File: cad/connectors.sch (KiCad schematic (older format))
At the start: 21 parts, among them J201 JACK_IN, J202 JACK_OUT, J203 CONN_PSU, J204 SW_BYPASS, J205 SW_FAT_A, J206 SW_EQ_A, J207 CONN_SIGNALS_A, J208 CONN_SW_EQ_A, K201 TQ2SA-5V, Q201 DTC123Y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

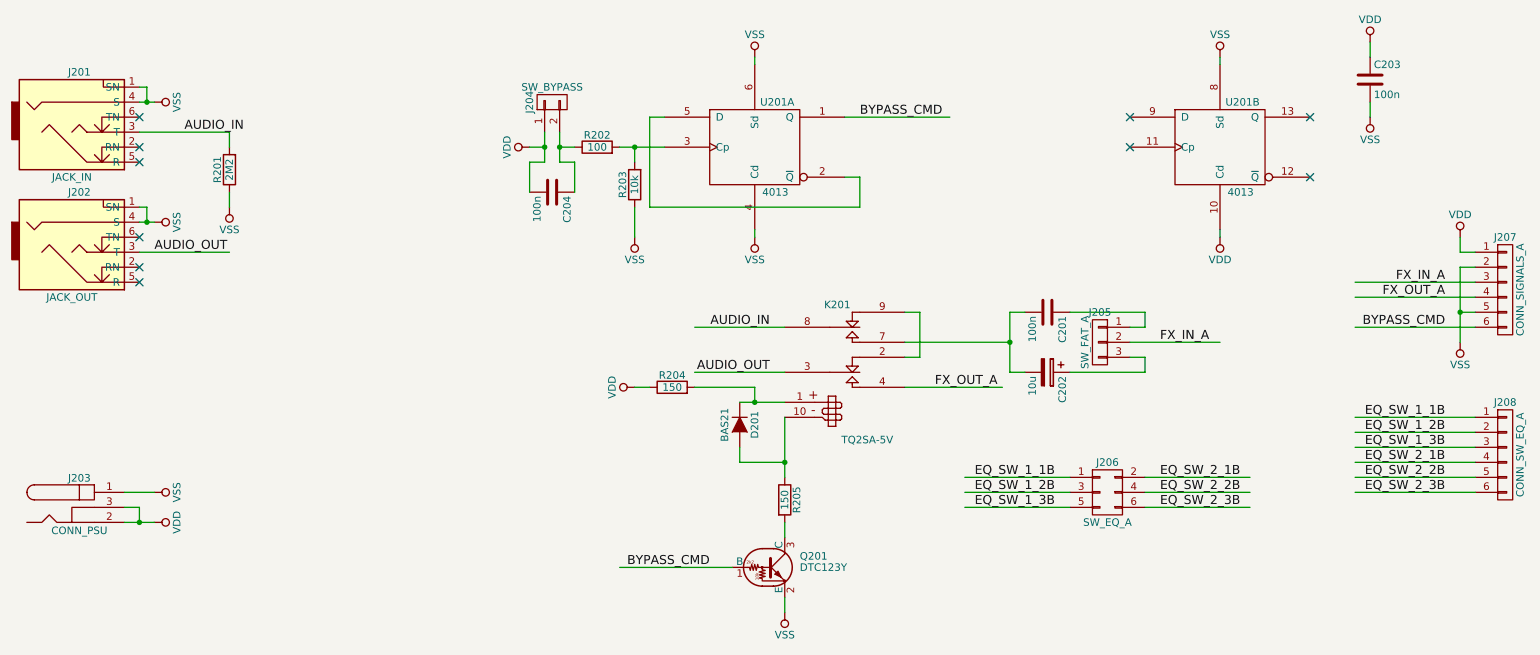
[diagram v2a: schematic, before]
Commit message: Corrected layout
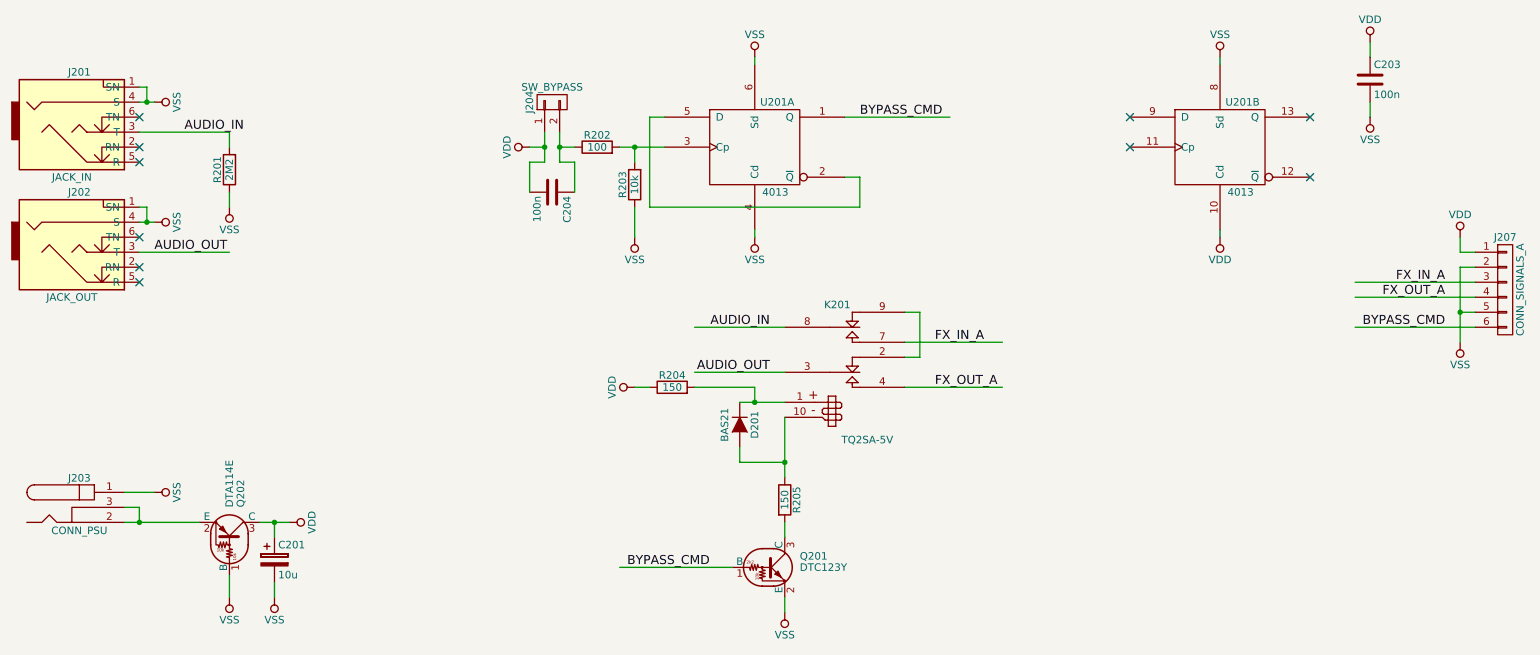
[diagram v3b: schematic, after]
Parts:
- removed C201: 100n, Capacitors_SMD:C_0603, symbol C
- removed C202: 10u, Capacitors_SMD:CP_Elec_4x4.5, symbol CP
- removed J205: SW_FAT_A, flax_lib:SW_SPDT_through_hole, symbol CONN_01X03
- removed J206: SW_EQ_A, flax_lib:SW_DPDT_through_hole, symbol CONN_02X03
- removed J208: CONN_SW_EQ_A, Pin_Headers:Pin_Header_Straight_1x06_Pitch1.27mm, symbol CONN_01X06
- added C201: 10u, Capacitors_SMD:CP_Elec_4x4.5, symbol CP
- added Q202: DTA114E, TO_SOT_Packages_SMD:SOT-23, symbol DTA114E
- J207: footprint Pin_Headers:Pin_Header_Straight_1x06_Pitch1.27mm -> Pin_Headers:Pin_Header_Straight_1x06_Pitch2.54mm
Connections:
- net labels removed: EQ_SW_1_1B, EQ_SW_1_2B, EQ_SW_1_3B, EQ_SW_2_1B, EQ_SW_2_2B, EQ_SW_2_3B
- wire segments 84 -> 66
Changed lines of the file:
@@
 LIBS:contrib
 LIBS:valves
+LIBS:flax_lib
 LIBS:hot_silicon_fuzz-cache
 EELAYER 25 0
@@
 L VDD #PWR02
 U 1 1 599D5C70
-P 1700 3900
-F 0 "#PWR02" H 1700 3750 50  0001 C CNN
-F 1 "VDD" H 1700 4050 50  0000 C CNN
-F 2 "" H 1700 3900 50  0001 C CNN
-F 3 "" H 1700 3900 50  0001 C CNN
-	1    1700 3900
+P 2600 3900
+F 0 "#PWR02" H 2600 3750 50  0001 C CNN
+F 1 "VDD" H 2600 4050 50  0000 C CNN
+F 2 "" H 2600 3900 50  0001 C CNN
+F 3 "" H 2600 3900 50  0001 C CNN
+	1    2600 3900
 	0    1    1    0
 $EndComp
@@
 Text Label 10300 2600 2    60   ~ 0
 BYPASS_CMD
-Text Label 8400 2700 0    60   ~ 0
+Text Label 6900 2700 0    60   ~ 0
 FX_IN_A
 Text Label 6900 3000 0    60   ~ 0
@@
 Text Label 5800 2900 2    60   ~ 0
 AUDIO_OUT
-$Comp
-L CONN_01X03 J205
-U 1 1 599E0F67
-P 8000 2700
-F 0 "J205" H 8000 2900 50  0000 C CNN
-F 1 "SW_FAT_A" V 8100 2700 50  0000 C CNN
-F 2 "flax_lib:SW_SPDT_through_hole" H 8000 2700 50  0001 C CNN
-F 3 "" H 8000 2700 50  0001 C CNN
-	1    8000 2700
-	-1   0    0    -1
-$EndComp
 Text Label 1900 1300 0    60   ~ 0
 AUDIO_IN
@@
 	1700 1100 1600 1100
 Wire Wire Line
-	1700 3900 1500 3900
+	1500 3900 2000 3900
 Wire Wire Line
 	1700 3700 1500 3700
@@
 Wire Wire Line
 	6800 2800 6700 2800
-Wire Wire Line
-	6700 2700 7400 2700
 Wire Wire Line
 	6700 3000 7350 3000
@@
 	1650 1800 1600 1800
 Connection ~ 1650 1900
-$Comp
-L C C201
-U 1 1 59A4C299
-P 7650 2500
-F 0 "C201" H 7675 2600 50  0000 L CNN
-F 1 "100n" H 7675 2400 50  0000 L CNN
-F 2 "Capacitors_SMD:C_0603" H 7688 2350 50  0001 C CNN
-F 3 "" H 7650 2500 50  0001 C CNN
-	1    7650 2500
-	0    1    1    0
-$EndComp
-Wire Wire Line
-	7400 2500 7400 2900
-Wire Wire Line
-	7400 2500 7500 2500
-$Comp
-L CP C202
-U 1 1 59A4C4B8
-P 7650 2900
-F 0 "C202" H 7675 3000 50  0000 L CNN
-F 1 "10u" H 7675 2800 50  0000 L CNN
-F 2 "Capacitors_SMD:CP_Elec_4x4.5" H 7688 2750 50  0001 C CNN
-F 3 "" H 7650 2900 50  0001 C CNN
-	1    7650 2900
-	0    1    1    0
-$EndComp
-Wire Wire Line
-	7400 2900 7500 2900
-Connection ~ 7400 2700
-Wire Wire Line
-	8200 2700 8800 2700
-Wire Wire Line
-	8200 2600 8300 2600
-Wire Wire Line
-	8300 2600 8300 2500
-Wire Wire Line
-	8300 2500 7800 2500
-Wire Wire Line
-	7800 2900 8300 2900
-Wire Wire Line
-	8300 2900 8300 2800
-Wire Wire Line
-	8300 2800 8200 2800
 Wire Wire Line
 	9700 2300 10500 2300
@@
 F 0 "J207" H 10700 2700 50  0000 C CNN
 F 1 "CONN_SIGNALS_A" V 10800 2350 50  0000 C CNN
-F 2 "Pin_Headers:Pin_Header_Straight_1x06_Pitch1.27mm" H 10700 2350 50  0001 C CNN
+F 2 "Pin_Headers:Pin_Header_Straight_1x06_Pitch2.54mm" H 10700 2350 50  0001 C CNN
 F 3 "" H 10700 2350 50  0001 C CNN
 	1    10700 2350
@@
 	10500 2500 10400 2500
 Connection ~ 10400 2500
-Text Label 10300 3200 2    60   ~ 0
-EQ_SW_1_1B
-$Comp
-L CONN_01X06 J208
-U 1 1 59A529D0
-P 10700 3450
-F 0 "J208" H 10700 3800 50  0000 C CNN
-F 1 "CONN_SW_EQ_A" V 10800 3450 50  0000 C CNN
-F 2 "Pin_Headers:Pin_Header_Straight_1x06_Pitch1.27mm" H 10700 3450 50  0001 C CNN
-F 3 "" H 10700 3450 50  0001 C CNN
-	1    10700 3450
-	1    0    0    -1
-$EndComp
-Wire Wire Line
-	10500 3200 9700 3200
-Text Label 10300 3300 2    60   ~ 0
-EQ_SW_1_2B
-Text Label 10300 3400 2    60   ~ 0
-EQ_SW_1_3B
-Text Label 10300 3500 2    60   ~ 0
-EQ_SW_2_1B
-Wire Wire Line
-	10500 3500 9700 3500
-Text Label 10300 3600 2    60   ~ 0
-EQ_SW_2_2B
-Text Label 10300 3700 2    60   ~ 0
-EQ_SW_2_3B
-Wire Wire Line
-	10500 3300 9700 3300
-Wire Wire Line
-	9700 3400 10500 3400
-Wire Wire Line
-	10500 3600 9700 3600
-Wire Wire Line
-	9700 3700 10500 3700
-$Comp
-L CONN_02X03 J206
-U 1 1 59A53228
-P 8050 3700
-F 0 "J206" H 8050 3900 50  0000 C CNN
-F 1 "SW_EQ_A" H 8050 3500 50  0000 C CNN
-F 2 "flax_lib:SW_DPDT_through_hole" H 8050 2500 50  0001 C CNN
-F 3 "" H 8050 2500 50  0001 C CNN
-	1    8050 3700
-	1    0    0    -1
-$EndComp
-Text Label 7700 3600 2    60   ~ 0
-EQ_SW_1_1B
-Text Label 7700 3700 2    60   ~ 0
-EQ_SW_1_2B
-Text Label 7700 3800 2    60   ~ 0
-EQ_SW_1_3B
-Text Label 8400 3600 0    60   ~ 0
-EQ_SW_2_1B
-Text Label 8400 3700 0    60   ~ 0
-EQ_SW_2_2B
-Text Label 8400 3800 0    60   ~ 0
-EQ_SW_2_3B
-Wire Wire Line
-	7800 3600 7100 3600
-Wire Wire Line
-	7100 3700 7800 3700
-Wire Wire Line
-	7800 3800 7100 3800
-Wire Wire Line
-	8300 3600 9000 3600
-Wire Wire Line
-	8300 3700 9000 3700
-Wire Wire Line
-	8300 3800 9000 3800
 $Comp
 L R R204
@@
 	-1   0    0    1
 $EndComp
+$Comp
+L DTA114E Q202
+U 1 1 5A456CFE
+P 2200 4000
+F 0 "Q202" H 2400 4075 50  0000 L CNN
+F 1 "DTA114E" H 2400 4000 50  0000 L CNN
+F 2 "TO_SOT_Packages_SMD:SOT-23" H 2200 4000 50  0001 L CNN
+F 3 "" H 2200 4000 50  0001 L CNN
+	1    2200 4000
+	0    1    -1   0
+$EndComp
+$Comp
+L VSS #PWR018
+U 1 1 5A456E01
+P 2200 4400
+F 0 "#PWR018" H 2200 4250 50  0001 C CNN
+F 1 "VSS" H 2200 4550 50  0000 C CNN
+F 2 "" H 2200 4400 50  0001 C CNN
+F 3 "" H 2200 4400 50  0001 C CNN
+	1    2200 4400
+	-1   0    0    1
+$EndComp
+$Comp
+L CP C201
+U 1 1 5A457097
+P 2500 4150
+F 0 "C201" H 2525 4250 50  0000 L CNN
+F 1 "10u" H 2525 4050 50  0000 L CNN
+F 2 "Capacitors_SMD:CP_Elec_4x4.5" H 2538 4000 50  0001 C CNN
+F 3 "" H 2500 4150 50  0001 C CNN
+	1    2500 4150
+	1    0    0    -1
+$EndComp
+$Comp
+L VSS #PWR019
+U 1 1 5A45748B
+P 2500 4400
+F 0 "#PWR019" H 2500 4250 50  0001 C CNN
+F 1 "VSS" H 2500 4550 50  0000 C CNN
+F 2 "" H 2500 4400 50  0001 C CNN
+F 3 "" H 2500 4400 50  0001 C CNN
+	1    2500 4400
+	-1   0    0    1
+$EndComp
+Wire Wire Line
+	2500 4300 2500 4400
+Wire Wire Line
+	2200 4400 2200 4250
+Wire Wire Line
+	2600 3900 2400 3900
+Wire Wire Line
+	2500 4000 2500 3900
+Connection ~ 2500 3900
+Wire Wire Line
+	6700 2700 7350 2700
 $EndSCHEMATC
